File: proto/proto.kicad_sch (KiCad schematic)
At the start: 1 part

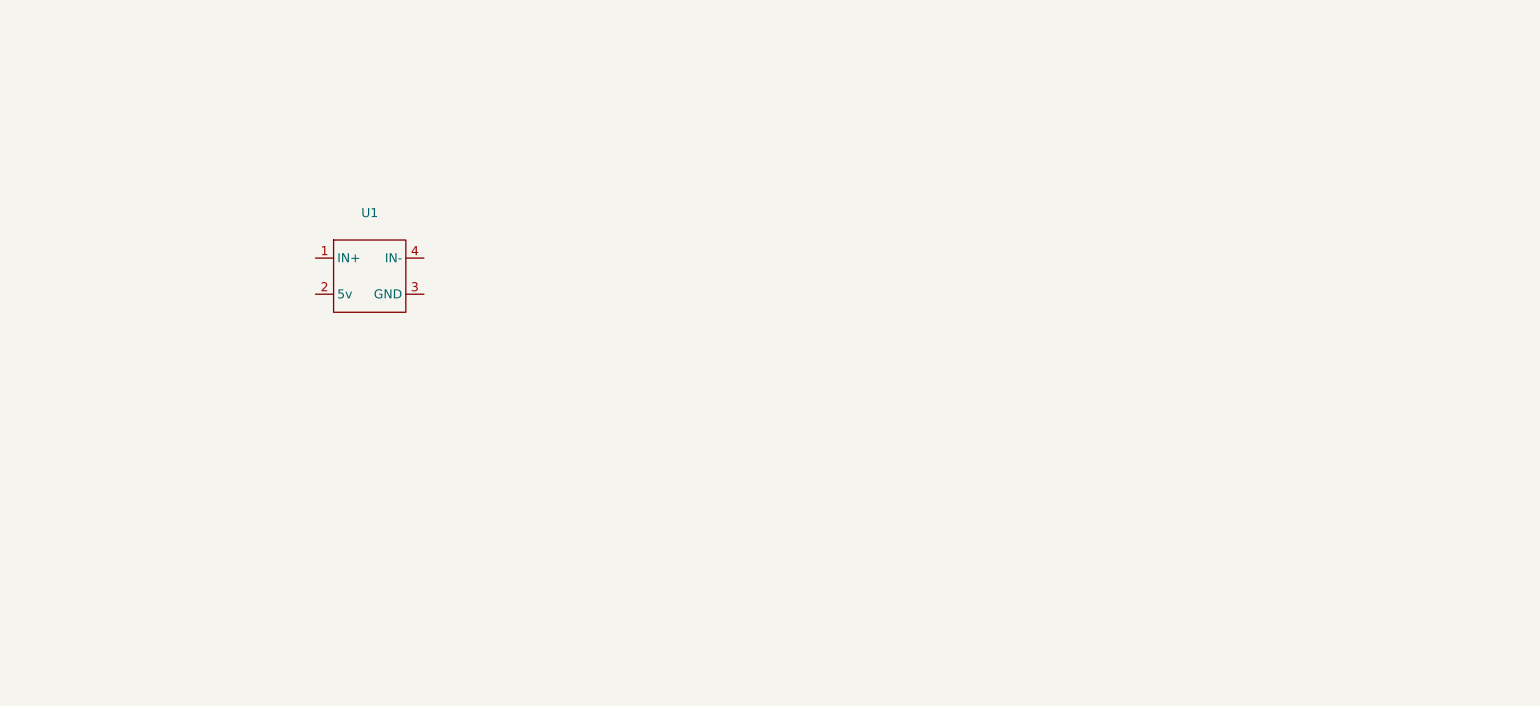
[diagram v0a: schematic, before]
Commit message: Ongoing development of prototype, symbols, footprints, and logic schematic
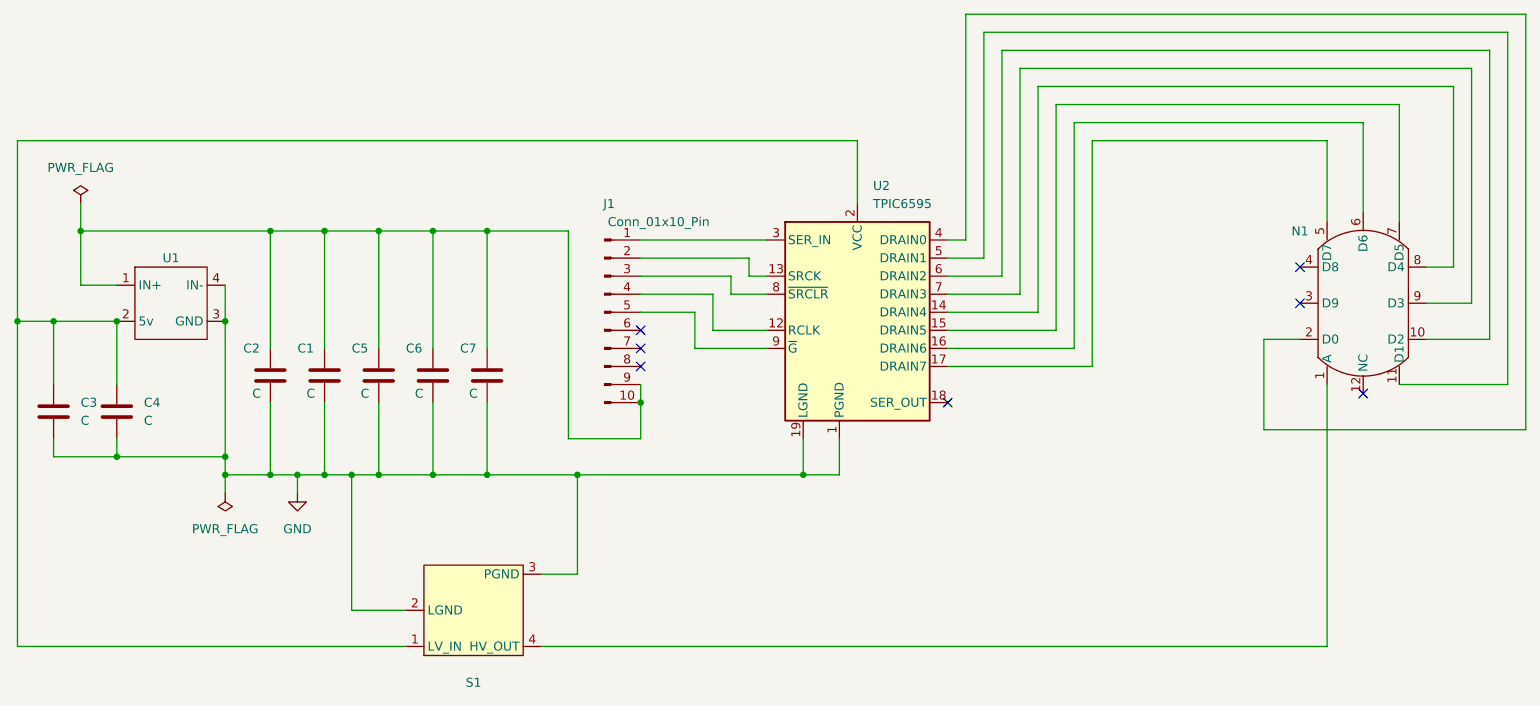
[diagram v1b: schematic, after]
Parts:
- added C1, C3: C, Capacitor_THT:CP_Radial_D5.0mm_P2.50mm, symbol Device:C
- added C2, C4, C5, C6, C7: C, Capacitor_THT:C_Disc_D3.0mm_W1.6mm_P2.50mm, symbol Device:C
- added J1: Conn_01x10_Pin, Connector_PinHeader_2.54mm:PinHeader_1x10_P2.54mm_Vertical, symbol Connector:Conn_01x10_Pin
- added N1: ~, NixComp:IN_12B_Socket, symbol NixComp:IN_12A
- added S1: ~, Package_DIP:DIP-14_W7.62mm_LongPads, symbol NixComp:NCH8200HV_170v
- added U2: TPIC6595, Package_DIP:DIP-20_W7.62mm_LongPads, symbol Interface_Expansion:TPIC6595
- U1: footprint (none) -> NixComp:TR4R7
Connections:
- net at U1.1 (IN+): now also C1.1, C2.1, C5.1, C6.1, C7.1, J1.10 (Pin_10), J1.9 (Pin_9)
- net at U1.2 (5v): now also C3.1, C4.1, S1.1 (LV_IN), U2.2 (VCC)
- net GND: now reaches U1.3 (GND)
- net GND: now also U1.4 (IN-), C1.2, C2.2, C3.2, C4.2, C5.2, C6.2, C7.2, S1.2 (LGND), S1.3 (PGND), U2.1 (PGND), U2.10 (PGND), U2.11 (PGND), U2.19 (LGND), U2.20 (PGND)
- new net: N1.1 (A), S1.4 (HV_OUT)
- new net: J1.4 (Pin_4), U2.12 (RCLK)
- new net: J1.2 (Pin_2), U2.13 (SRCK)
- new net: N1.8 (D4), U2.14 (DRAIN4)
- new net: N1.7 (D5), U2.15 (DRAIN5)
- new net: N1.6 (D6), U2.16 (DRAIN6)
- new net: N1.5 (D7), U2.17 (DRAIN7)
- new net: J1.1 (Pin_1), U2.3 (SER_IN)
- new net: N1.2 (D0), U2.4 (DRAIN0)
- new net: N1.11 (D1), U2.5 (DRAIN1)
- new net: N1.10 (D2), U2.6 (DRAIN2)
- new net: N1.9 (D3), U2.7 (DRAIN3)
- new net: J1.3 (Pin_3), U2.8 (~{SRCLR})
- new net: J1.5 (Pin_5), U2.9 (~{G})
- no-connect marks 0 -> 7
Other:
- moved on the sheet: U1

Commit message: Add footprint for socketed HV supply. Add R1 which was forgotten. Revise layout for significantly better density.
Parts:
- added R1: R, Resistor_THT:R_Axial_DIN0414_L11.9mm_D4.5mm_P15.24mm_Horizontal, symbol Device:R
- S1: footprint Package_DIP:DIP-14_W7.62mm_LongPads -> NixComp:NCH8200HV_Socket_LongPads
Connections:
- net at N1.1 (A): now also R1.1; no longer S1.4 (HV_OUT)
- new net: R1.2, S1.4 (HV_OUT)
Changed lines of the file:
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@@
-	(wire
-		(pts
-			(xy 205.74 73.66) (xy 205.74 110.49)
-		)
-		(stroke
-			(width 0)
-			(type default)
-		)
-	)
 	(wire
 		(pts
@@
 	(wire
 		(pts
+			(xy 205.74 73.66) (xy 205.74 87.63)
+		)
+		(stroke
+			(width 0)
+			(type default)
+		)
+	)
+	(wire
+		(pts
 			(xy 99.06 81.28) (xy 109.22 81.28)
 		)
@@
 	(wire
 		(pts
+			(xy 205.74 95.25) (xy 205.74 110.49)
+		)
+		(stroke
+			(width 0)
+			(type default)
+		)
+	)
+	(wire
+		(pts
 			(xy 223.52 31.75) (xy 223.52 57.15)
 		)
@@
 			(width 0)
 			(type default)
+		)
+	)
+	(symbol
+		(lib_id "Device:R")
+		(at 205.74 91.44 0)
+		(unit 1)
+		(exclude_from_sim no)
+		(in_bom yes)
+		(on_board yes)
+		(dnp no)
+		(fields_autoplaced yes)
+		(property "Reference" "R1"
+			(at 208.28 90.1699 0)
+			(effects
+				(font
+					(size 1.27 1.27)
+				)
+				(justify left)
+			)
+		)
+		(property "Value" "R"
+			(at 208.28 92.7099 0)
+			(effects
+				(font
+					(size 1.27 1.27)
+				)
+				(justify left)
+			)
+		)
+		(property "Footprint" "Resistor_THT:R_Axial_DIN0414_L11.9mm_D4.5mm_P15.24mm_Horizontal"
+			(at 203.962 91.44 90)
+			(effects
+				(font
+					(size 1.27 1.27)
+				)
+				(hide yes)
+			)
+		)
+		(property "Datasheet" "~"
+			(at 205.74 91.44 0)
+			(effects
+				(font
+					(size 1.27 1.27)
+				)
+				(hide yes)
+			)
+		)
+		(property "Description" "Resistor"
+			(at 205.74 91.44 0)
+			(effects
+				(font
+					(size 1.27 1.27)
+				)
+				(hide yes)
+			)
+		)
+		(pin "2"
+		)
+		(pin "1"
+		)
+		(instances
+			(project ""
+				(path "/2149644b-a7a7-4a4b-a38a-471f6dd87e38"
+					(reference "R1")
+					(unit 1)
+				)
+			)
 		)
 	)
@@
 			)
 		)
-		(property "Footprint" "Package_DIP:DIP-14_W7.62mm_LongPads"
+		(property "Footprint" "NixComp:NCH8200HV_Socket_LongPads"
 			(at 87.63 105.41 0)
 			(effects

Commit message: Ongoing development
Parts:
- added J2, J3, J4, J5: Conn_01x05_Pin, Connector_PinHeader_2.54mm:PinHeader_1x05_P2.54mm_Vertical, symbol Connector:Conn_01x05_Pin
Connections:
- net GND: now also J3.1 (Pin_1), J3.2 (Pin_2), J3.3 (Pin_3), J3.4 (Pin_4), J3.5 (Pin_5), J4.1 (Pin_1), J4.2 (Pin_2), J4.3 (Pin_3), J4.4 (Pin_4), J4.5 (Pin_5)
- net at C3.1, C4.1, S1.1 (LV_IN)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: now also C6.1, C7.1, J5.1 (Pin_1), J5.2 (Pin_2), J5.3 (Pin_3), J5.4 (Pin_4), J5.5 (Pin_5)
- net at C1.1, C2.1, C5.1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: now also J2.1 (Pin_1), J2.2 (Pin_2), J2.3 (Pin_3), J2.4 (Pin_4), J2.5 (Pin_5); no longer C6.1, C7.1, J1.10 (Pin_10), J1.9 (Pin_9)
- net at U2.12 (RCLK): now also J1.6 (Pin_6); no longer J1.4 (Pin_4)
- net at U2.13 (SRCK): now also J1.3 (Pin_3); no longer J1.2 (Pin_2)
- net at U2.8 (~{SRCLR}): now also J1.4 (Pin_4); no longer J1.3 (Pin_3)
- net at U2.9 (~{G}): now also J1.7 (Pin_7); no longer J1.5 (Pin_5)
- no-connect marks 7 -> 9
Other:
- moved on the sheet: J1

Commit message: Improve footprint for pin connectors and align four power and ground connectors (I hope)
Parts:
- J2, J3, J4, J5: footprint Connector_PinHeader_2.54mm:PinHeader_1x05_P2.54mm_Vertical -> NixComp:PinHeader_1x05_P2.54mm_Vertical_SmallCourt
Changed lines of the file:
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@@
 			)
 		)
-		(property "Footprint" "Connector_PinHeader_2.54mm:PinHeader_1x05_P2.54mm_Vertical"
+		(property "Footprint" "NixComp:PinHeader_1x05_P2.54mm_Vertical_SmallCourt"
 			(at 35.56 97.79 0)
 			(effects
@@
 			)
 		)
-		(property "Footprint" "Connector_PinHeader_2.54mm:PinHeader_1x05_P2.54mm_Vertical"
+		(property "Footprint" "NixComp:PinHeader_1x05_P2.54mm_Vertical_SmallCourt"
 			(at 82.55 57.15 0)
 			(effects
@@
 			)
 		)
-		(property "Footprint" "Connector_PinHeader_2.54mm:PinHeader_1x05_P2.54mm_Vertical"
+		(property "Footprint" "NixComp:PinHeader_1x05_P2.54mm_Vertical_SmallCourt"
 			(at 149.86 86.36 0)
 			(effects
@@
 			)
 		)
-		(property "Footprint" "Connector_PinHeader_2.54mm:PinHeader_1x05_P2.54mm_Vertical"
+		(property "Footprint" "NixComp:PinHeader_1x05_P2.54mm_Vertical_SmallCourt"
 			(at 149.86 101.6 0)
 			(effects

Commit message: Ongoing development. Add ground vias.
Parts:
- removed J1: Conn_01x10_Pin, Connector_PinHeader_2.54mm:PinHeader_1x10_P2.54mm_Vertical, symbol Connector:Conn_01x10_Pin
- added J1: Conn_01x05_Pin, NixComp:PinHeader_1x05_P2.54mm_Vertical_SmallCourt, symbol Connector:Conn_01x05_Pin
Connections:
- net at U2.12 (RCLK): now also J1.4 (Pin_4)
- net at U2.13 (SRCK): now also J1.2 (Pin_2)
- net at U2.3 (SER_IN): now also J1.1 (Pin_1)
- net at U2.8 (~{SRCLR}): now also J1.3 (Pin_3)
- net at U2.9 (~{G}): now also J1.5 (Pin_5)
- no-connect marks 9 -> 4
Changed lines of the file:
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@@
-	)
-	(no_connect
-		(at 123.19 73.66)
 	)
 	(no_connect
@@
 	)
 	(no_connect
-		(at 123.19 63.5)
-	)
-	(no_connect
-		(at 123.19 71.12)
-	)
-	(no_connect
-		(at 123.19 55.88)
-	)
-	(no_connect
 		(at 152.4 76.2)
 	)
@@
 	)
 	(no_connect
-		(at 123.19 76.2)
-	)
-	(no_connect
 		(at 201.93 62.23)
 	)
 	(wire
 		(pts
+			(xy 121.92 53.34) (xy 127 53.34)
+		)
+		(stroke
+			(width 0)
+			(type default)
+		)
+	)
+	(wire
+		(pts
 			(xy 30.48 95.25) (xy 30.48 97.79)
 		)
@@
 	(wire
 		(pts
+			(xy 120.65 58.42) (xy 127 58.42)
+		)
+		(stroke
+			(width 0)
+			(type default)
+		)
+	)
+	(wire
+		(pts
 			(xy 77.47 54.61) (xy 77.47 57.15)
 		)
@@
 	(wire
 		(pts
+			(xy 120.65 55.88) (xy 121.92 55.88)
+		)
+		(stroke
+			(width 0)
+			(type default)
+		)
+	)
+	(wire
+		(pts
+			(xy 120.65 66.04) (xy 121.92 66.04)
+		)
+		(stroke
+			(width 0)
+			(type default)
+		)
+	)
+	(wire
+		(pts
 			(xy 72.39 52.07) (xy 77.47 52.07)
 		)
@@
 	(wire
 		(pts
-			(xy 123.19 58.42) (xy 127 58.42)
-		)
-		(stroke
-			(width 0)
-			(type default)
-		)
-	)
-	(wire
-		(pts
 			(xy 57.15 52.07) (xy 30.48 52.07)
 		)
@@
 	(wire
 		(pts
-			(xy 123.19 53.34) (xy 127 53.34)
-		)
-		(stroke
-			(width 0)
-			(type default)
-		)
-	)
-	(wire
-		(pts
 			(xy 219.71 67.31) (xy 228.6 67.31)
 		)
@@
 	(wire
 		(pts
+			(xy 120.65 63.5) (xy 124.46 63.5)
+		)
+		(stroke
+			(width 0)
+			(type default)
+		)
+	)
+	(wire
+		(pts
 			(xy 157.48 55.88) (xy 157.48 24.13)
 		)
@@
 	(wire
 		(pts
-			(xy 123.19 66.04) (xy 127 66.04)
-		)
-		(stroke
-			(width 0)
-			(type default)
-		)
-	)
-	(wire
-		(pts
 			(xy 157.48 24.13) (xy 231.14 24.13)
 		)
@@
 	(wire
 		(pts
+			(xy 121.92 55.88) (xy 121.92 53.34)
+		)
+		(stroke
+			(width 0)
+			(type default)
+		)
+	)
+	(wire
+		(pts
 			(xy 144.78 81.28) (xy 140.97 81.28)
 		)
@@
 	(wire
 		(pts
+			(xy 124.46 66.04) (xy 124.46 63.5)
+		)
+		(stroke
+			(width 0)
+			(type default)
+		)
+	)
+	(wire
+		(pts
 			(xy 144.78 91.44) (xy 144.78 96.52)
 		)
@@
 	(wire
 		(pts
-			(xy 123.19 68.58) (xy 127 68.58)
+			(xy 121.92 68.58) (xy 127 68.58)
+		)
+		(stroke
+			(width 0)
+			(type default)
+		)
+	)
+	(wire
+		(pts
+			(xy 120.65 60.96) (xy 127 60.96)
 		)
 		(stroke
@@
 	(wire
 		(pts
-			(xy 123.19 60.96) (xy 127 60.96)
+			(xy 127 66.04) (xy 124.46 66.04)
 		)
 		(stroke
@@
 		(pts
 			(xy 57.15 76.2) (xy 57.15 86.36)
+		)
+		(stroke
+			(width 0)
+			(type default)
+		)
+	)
+	(wire
+		(pts
+			(xy 121.92 68.58) (xy 121.92 66.04)
 		)
 		(stroke
@@
 	)
 	(symbol
+		(lib_id "Connector:Conn_01x05_Pin")
+		(at 115.57 60.96 0)
+		(unit 1)
+		(exclude_from_sim no)
+		(in_bom yes)
+		(on_board yes)
+		(dnp no)
+		(property "Reference" "J1"
+			(at 118.11 53.34 0)
+			(effects
+				(font
+					(size 1.27 1.27)
+				)
+				(justify right)
+			)
+		)
+		(property "Value" "Conn_01x05_Pin"
+			(at 127 71.12 0)
+			(effects
+				(font
+					(size 1.27 1.27)
+				)
+				(justify right)
+			)
+		)
+		(property "Footprint" "NixComp:PinHeader_1x05_P2.54mm_Vertical_SmallCourt"
+			(at 115.57 60.96 0)
+			(effects
+				(font
+					(size 1.27 1.27)
+				)
+				(hide yes)
+			)
+		)
+		(property "Datasheet" "~"
+			(at 115.57 60.96 0)
+			(effects
+				(font
+					(size 1.27 1.27)
+				)
+				(hide yes)
+			)
+		)
+		(property "Description" "Generic connector, single row, 01x05, script generated"
+			(at 115.57 60.96 0)
+			(effects
+				(font
+					(size 1.27 1.27)
+				)
+				(hide yes)
+			)
+		)
+		(pin "2"
+		)
+		(pin "3"
+		)
+		(pin "4"
+		)
+		(pin "5"
+		)
+		(pin "1"
+		)
+		(instances
+			(project "proto"
+				(path "/2149644b-a7a7-4a4b-a38a-471f6dd87e38"
+					(reference "J1")
+					(unit 1)
+				)
+			)
+		)
+	)
+	(symbol
 		(lib_id "power:PWR_FLAG")
 		(at 50.8 88.9 180)
@@
 					(unit 1)
 				)
-			)
-		)
-	)
-	(symbol
-		(lib_id "Connector:Conn_01x10_Pin")
-		(at 118.11 63.5 0)
-		(unit 1)
-		(exclude_from_sim no)
-		(in_bom yes)
-		(on_board yes)
-		(dnp no)
-		(property "Reference" "J1"
-			(at 120.65 49.53 0)
-			(effects
-				(font
-					(size 1.27 1.27)
-				)
-			)
-		)
-		(property "Value" "Conn_01x10_Pin"
-			(at 120.65 78.74 0)
-			(effects
-				(font
-					(size 1.27 1.27)
-				)
-			)
-		)
-		(property "Footprint" "Connector_PinHeader_2.54mm:PinHeader_1x10_P2.54mm_Vertical"
-			(at 118.11 63.5 0)
-			(effects
-				(font
-					(size 1.27 1.27)
-				)
-				(hide yes)
-			)
-		)
-		(property "Datasheet" "~"
-			(at 118.11 63.5 0)
-			(effects
-				(font
-					(size 1.27 1.27)
-				)
-				(hide yes)
-			)
-		)
-		(property "Description" "Generic connector, single row, 01x10, script generated"
-			(at 118.11 63.5 0)
-			(effects
-				(font
-					(size 1.27 1.27)
-				)
-				(hide yes)
-			)
-		)
-		(pin "1"
-		)
-		(pin "10"
-		)
-		(pin "3"
-		)
-		(pin "5"
-		)
-		(pin "6"
-		)
-		(pin "7"
-		)
-		(pin "8"
-		)
-		(pin "9"
-		)
-		(pin "2"
-		)
-		(pin "4"
-		)
-		(instances
-			(project ""
-				(path "/2149644b-a7a7-4a4b-a38a-471f6dd87e38"
-					(reference "J1")
-					(unit 1)
-				)

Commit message: Completely revise high voltage converter footprint and circuit du to previous errors. Generate Gerbers. Some issues remain.
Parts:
- J1: value Conn_01x05_Pin -> J1
- J2: value Conn_01x05_Pin -> J2
- J3: value Conn_01x05_Pin -> J3
- J4: value Conn_01x05_Pin -> J4
- J5: value Conn_01x05_Pin -> J5
- S1: value ~ -> NCH8200HV; footprint NixComp:NCH8200HV_Socket_LongPads -> NixComp:NCH8200HV
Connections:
- net GND: now also S1.4 (PGND); no longer S1.2 (LGND)
- net at R1.2: now also S1.1 (HV_OUT); no longer S1.4 (HV_OUT)
- net at C3.1, C4.1, C6.1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: now also S1.2 (LV_IN); no longer S1.1 (LV_IN)
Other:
- note added: "170V"
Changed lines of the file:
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@@
-	)
-	(junction
-		(at 100.33 86.36)
-		(diameter 0)
-		(color 0 0 0 0)
 	)
 	(junction
@@
 	)
 	(junction
+		(at 99.06 86.36)
+		(diameter 0)
+		(color 0 0 0 0)
+	)
+	(junction
 		(at 144.78 91.44)
 		(diameter 0)
@@
 	)
 	(junction
+		(at 99.06 102.87)
+		(diameter 0)
+		(color 0 0 0 0)
+	)
+	(junction
 		(at 144.78 86.36)
 		(diameter 0)
@@
 	(junction
 		(at 60.96 86.36)
-		(diameter 0)
-		(color 0 0 0 0)
-	)
-	(junction
-		(at 68.58 86.36)
 		(diameter 0)
 		(color 0 0 0 0)
@@
 	(wire
 		(pts
+			(xy 99.06 86.36) (xy 104.14 86.36)
+		)
+		(stroke
+			(width 0)
+			(type default)
+		)
+	)
+	(wire
+		(pts
 			(xy 50.8 88.9) (xy 50.8 86.36)
 		)
@@
 	(wire
 		(pts
-			(xy 100.33 86.36) (xy 100.33 100.33)
+			(xy 68.58 102.87) (xy 68.58 115.57)
 		)
 		(stroke
@@
 	(wire
 		(pts
+			(xy 93.98 110.49) (xy 99.06 110.49)
+		)
+		(stroke
+			(width 0)
+			(type default)
+		)
+	)
+	(wire
+		(pts
 			(xy 26.67 64.77) (xy 26.67 73.66)
 		)
@@
 	(wire
 		(pts
-			(xy 95.25 110.49) (xy 205.74 110.49)
-		)
-		(stroke
-			(width 0)
-			(type default)
-		)
-	)
-	(wire
-		(pts
 			(xy 77.47 52.07) (xy 77.47 54.61)
 		)
@@
 	(wire
 		(pts
-			(xy 76.2 110.49) (xy 21.59 110.49)
-		)
-		(stroke
-			(width 0)
-			(type default)
-		)
-	)
-	(wire
-		(pts
-			(xy 100.33 86.36) (xy 104.14 86.36)
-		)
-		(stroke
-			(width 0)
-			(type default)
-		)
-	)
-	(wire
-		(pts
-			(xy 68.58 86.36) (xy 68.58 105.41)
-		)
-		(stroke
-			(width 0)
-			(type default)
-		)
-	)
-	(wire
-		(pts
 			(xy 231.14 24.13) (xy 231.14 73.66)
 		)
@@
 	(wire
 		(pts
+			(xy 99.06 102.87) (xy 99.06 110.49)
+		)
+		(stroke
+			(width 0)
+			(type default)
+		)
+	)
+	(wire
+		(pts
 			(xy 21.59 92.71) (xy 30.48 92.71)
 		)
@@
 	(wire
 		(pts
-			(xy 64.77 86.36) (xy 68.58 86.36)
+			(xy 64.77 86.36) (xy 72.39 86.36)
 		)
 		(stroke
@@
 	(wire
 		(pts
+			(xy 74.93 110.49) (xy 21.59 110.49)
+		)
+		(stroke
+			(width 0)
+			(type default)
+		)
+	)
+	(wire
+		(pts
 			(xy 165.1 31.75) (xy 223.52 31.75)
 		)
@@
 	(wire
 		(pts
+			(xy 93.98 102.87) (xy 99.06 102.87)
+		)
+		(stroke
+			(width 0)
+			(type default)
+		)
+	)
+	(wire
+		(pts
 			(xy 154.94 53.34) (xy 154.94 21.59)
 		)
@@
 	(wire
 		(pts
+			(xy 99.06 102.87) (xy 99.06 86.36)
+		)
+		(stroke
+			(width 0)
+			(type default)
+		)
+	)
+	(wire
+		(pts
 			(xy 144.78 81.28) (xy 140.97 81.28)
 		)
@@
 	(wire
 		(pts
-			(xy 68.58 86.36) (xy 72.39 86.36)
-		)
-		(stroke
-			(width 0)
-			(type default)
-		)
-	)
-	(wire
-		(pts
 			(xy 60.96 86.36) (xy 64.77 86.36)
 		)
@@
 	(wire
 		(pts
-			(xy 72.39 86.36) (xy 100.33 86.36)
+			(xy 72.39 86.36) (xy 99.06 86.36)
 		)
 		(stroke
@@
 	(wire
 		(pts
+			(xy 68.58 115.57) (xy 205.74 115.57)
+		)
+		(stroke
+			(width 0)
+			(type default)
+		)
+	)
+	(wire
+		(pts
 			(xy 120.65 60.96) (xy 127 60.96)
 		)
@@
 	(wire
 		(pts
-			(xy 95.25 100.33) (xy 100.33 100.33)
-		)
-		(stroke
-			(width 0)
-			(type default)
-		)
-	)
-	(wire
-		(pts
 			(xy 127 66.04) (xy 124.46 66.04)
 		)
@@
 	(wire
 		(pts
-			(xy 205.74 95.25) (xy 205.74 110.49)
+			(xy 205.74 95.25) (xy 205.74 115.57)
 		)
 		(stroke
@@
 	(wire
 		(pts
-			(xy 76.2 105.41) (xy 68.58 105.41)
-		)
-		(stroke
-			(width 0)
-			(type default)
-		)
-	)
-	(wire
-		(pts
 			(xy 231.14 73.66) (xy 215.9 73.66)
 		)
@@
 			(width 0)
 			(type default)
+		)
+	)
+	(wire
+		(pts
+			(xy 74.93 102.87) (xy 68.58 102.87)
+		)
+		(stroke
+			(width 0)
+			(type default)
+		)
+	)
+	(text "170V"
+		(exclude_from_sim no)
+		(at 127 114.3 0)
+		(effects
+			(font
+				(size 1.27 1.27)
+			)
 		)
 	)
@@
 			)
 		)
-		(property "Value" "Conn_01x05_Pin"
-			(at 27.94 105.41 0)
+		(property "Value" "J5"
+			(at 31.75 105.41 0)
 			(effects
 				(font
@@
 			)
 		)
-		(property "Value" "Conn_01x05_Pin"
-			(at 74.93 64.77 0)
+		(property "Value" "J2"
+			(at 78.74 64.77 0)
 			(effects
 				(font
@@
 				(path "/2149644b-a7a7-4a4b-a38a-471f6dd87e38"
 					(reference "J2")
-					(unit 1)
-				)
-			)
-		)
-	)
-	(symbol
-		(lib_id "NixComp:NCH8200HV_170v")
-		(at 86.36 105.41 0)
-		(mirror x)
-		(unit 1)
-		(exclude_from_sim no)
-		(in_bom yes)
-		(on_board yes)
-		(dnp no)
-		(property "Reference" "S1"
-			(at 85.725 115.57 0)
-			(effects
-				(font
-					(size 1.27 1.27)
-				)
-			)
-		)
-		(property "Value" "~"
-			(at 85.725 113.03 0)
-			(effects
-				(font
-					(size 1.27 1.27)
-				)
-			)
-		)
-		(property "Footprint" "NixComp:NCH8200HV_Socket_LongPads"
-			(at 87.63 105.41 0)
-			(effects
-				(font
-					(size 1.27 1.27)
-				)
-				(hide yes)
-			)
-		)
-		(property "Datasheet" ""
-			(at 87.63 105.41 0)
-			(effects
-				(font
-					(size 1.27 1.27)
-				)
-				(hide yes)
-			)
-		)
-		(property "Description" ""
-			(at 87.63 105.41 0)
-			(effects
-				(font
-					(size 1.27 1.27)
-				)
-				(hide yes)
-			)
-		)
-		(pin "3"
-		)
-		(pin "2"
-		)
-		(pin "1"
-		)
-		(pin "4"
-		)
-		(instances
-			(project ""
-				(path "/2149644b-a7a7-4a4b-a38a-471f6dd87e38"
-					(reference "S1")
 					(unit 1)
 				)
@@
 	)
 	(symbol
+		(lib_id "NixComp:NCH8200HV_170v")
+		(at 85.09 106.68 0)
+		(unit 1)
+		(exclude_from_sim no)
+		(in_bom yes)
+		(on_board yes)
+		(dnp no)
+		(fields_autoplaced yes)
+		(property "Reference" "S1"
+			(at 84.455 95.25 0)
+			(effects
+				(font
+					(size 1.27 1.27)
+				)
+			)
+		)
+		(property "Value" "NCH8200HV"
+			(at 84.455 97.79 0)
+			(effects
+				(font
+					(size 1.27 1.27)
+				)
+			)
+		)
+		(property "Footprint" "NixComp:NCH8200HV"
+			(at 86.36 106.68 0)
+			(effects
+				(font
+					(size 1.27 1.27)
+				)
+				(hide yes)
+			)
+		)
+		(property "Datasheet" ""
+			(at 86.36 106.68 0)
+			(effects
+				(font
+					(size 1.27 1.27)
+				)
+				(hide yes)
+			)
+		)
+		(property "Description" ""
+			(at 86.36 106.68 0)
+			(effects
+				(font
+					(size 1.27 1.27)
+				)
+				(hide yes)
+			)
+		)
+		(pin "3"
+		)
+		(pin "4"
+		)
+		(pin "2"
+		)
+		(pin "1"
+		)
+		(instances
+			(project ""
+				(path "/2149644b-a7a7-4a4b-a38a-471f6dd87e38"
+					(reference "S1")
+					(unit 1)
+				)
+			)
+		)
+	)
+	(symbol
 		(lib_id "Connector:Conn_01x05_Pin")
 		(at 149.86 86.36 180)
@@
 			)
 		)
-		(property "Value" "Conn_01x05_Pin"
+		(property "Value" "J3"
 			(at 151.13 87.6299 0)
 			(effects
@@
 			)
 		)
-		(property "Value" "Conn_01x05_Pin"
+		(property "Value" "J4"
 			(at 151.13 102.8699 0)
 			(effects
@@
 			)
 		)
-		(property "Value" "Conn_01x05_Pin"
-			(at 127 71.12 0)
-			(effects
-				(font
+		(property "Value" "J1"
+			(at 118.11 68.58 0)
+			(effects
+				(font
